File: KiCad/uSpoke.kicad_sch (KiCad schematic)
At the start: 68 parts, among them J1 SM12B-SRSS-TB, J12 Amphenol 132289, J2 PLS-1x3, J4 PLS-1x3, Q2 AO3407A, Q3 AO3400, Q5 AO3400, U1 SP0503BAHTG, U2 TP4056, U4 LM3671MF-3.3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

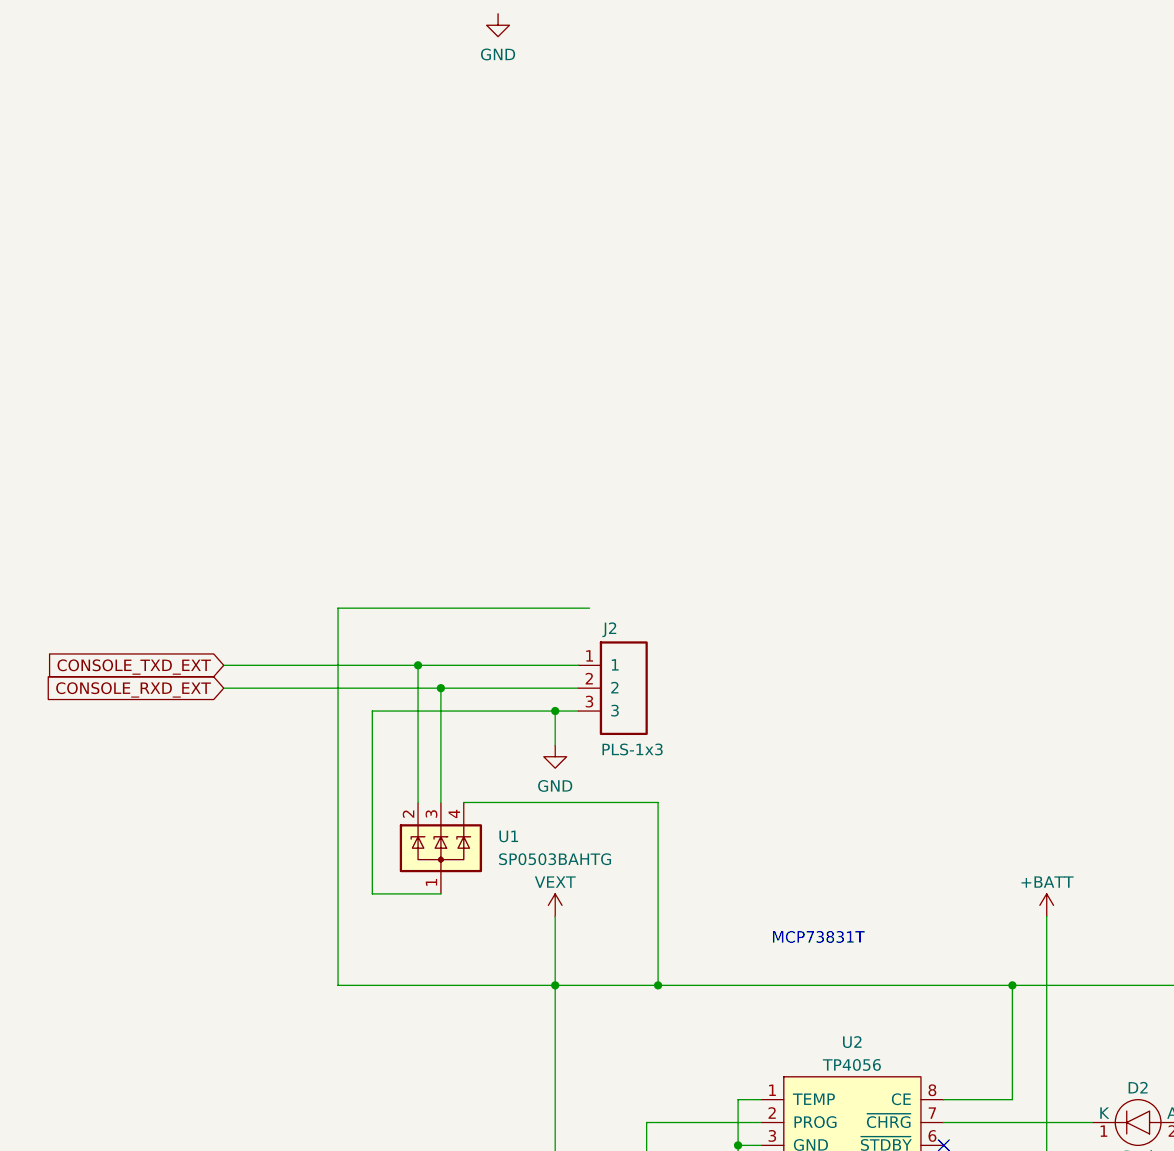
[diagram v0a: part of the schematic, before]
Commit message: Add 1x4 header (magnetic pogo)
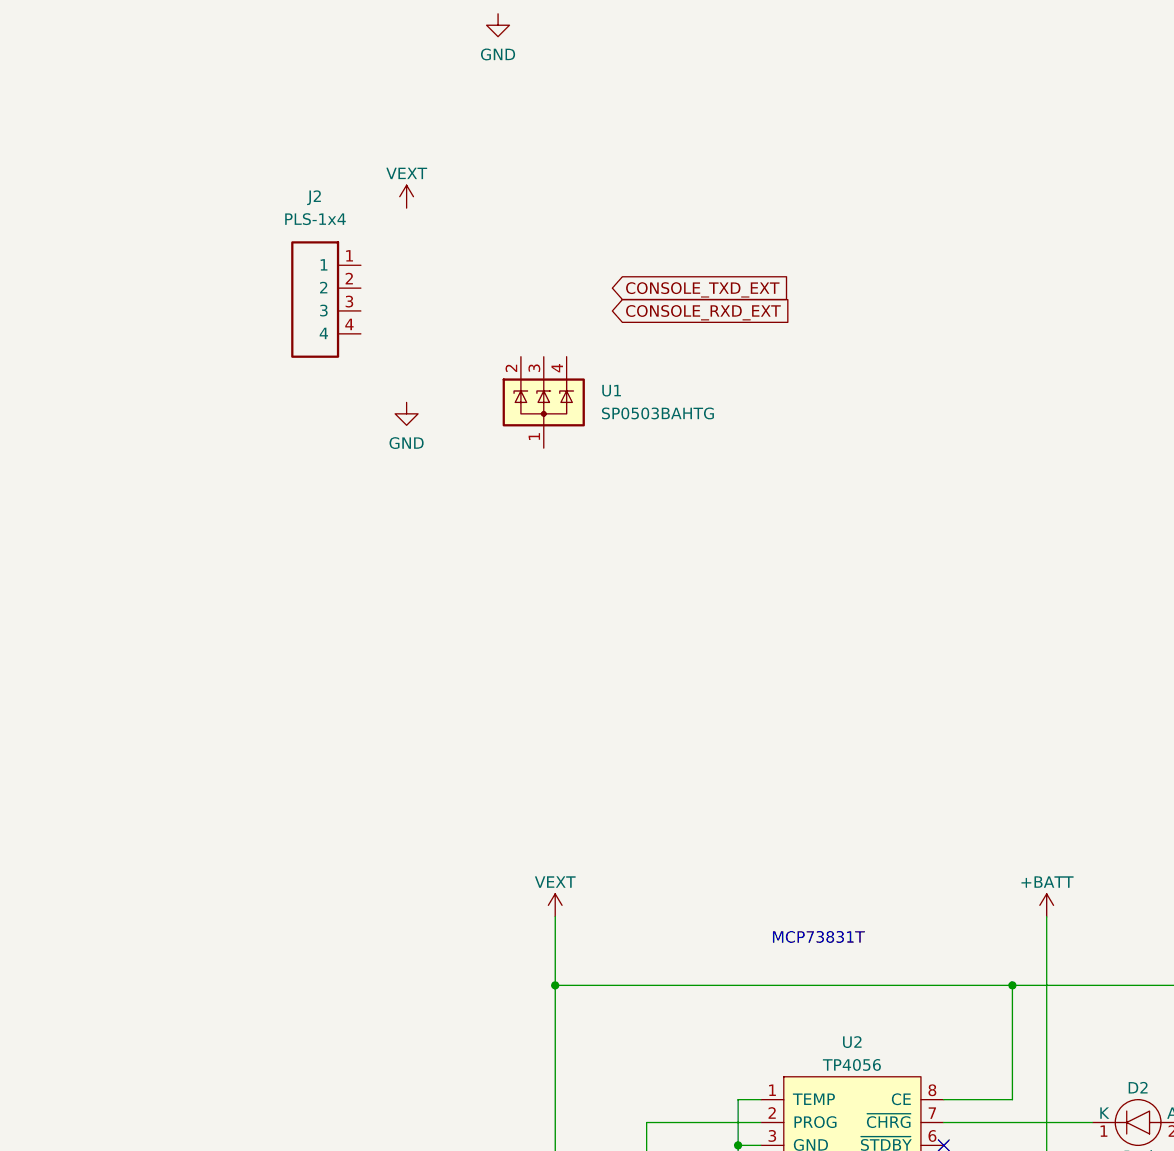
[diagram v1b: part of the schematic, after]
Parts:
- removed J2: PLS-1x3, Spoke:Header_1x3, symbol Spoke:PLS-1x3
- added J2: PLS-1x4, symbol uSpoke:PLS-1x4
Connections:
- net CONSOLE_RXD_EXT: no longer U1.3 (K)
- net CONSOLE_TXD_EXT: no longer U1.2 (K)
- net GND: no longer U1.1 (A)
- net VEXT: no longer U1.4 (K)
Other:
- moved on the sheet: U1

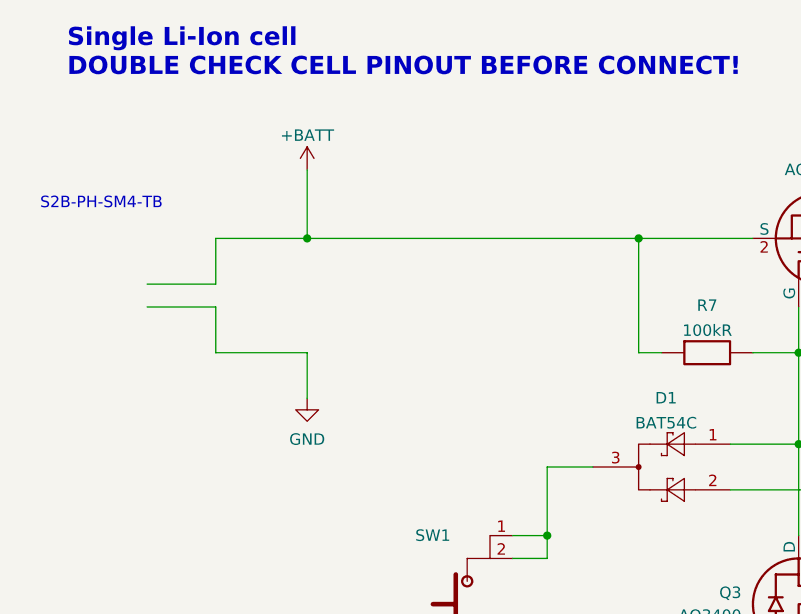
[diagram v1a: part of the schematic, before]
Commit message: Update SMA
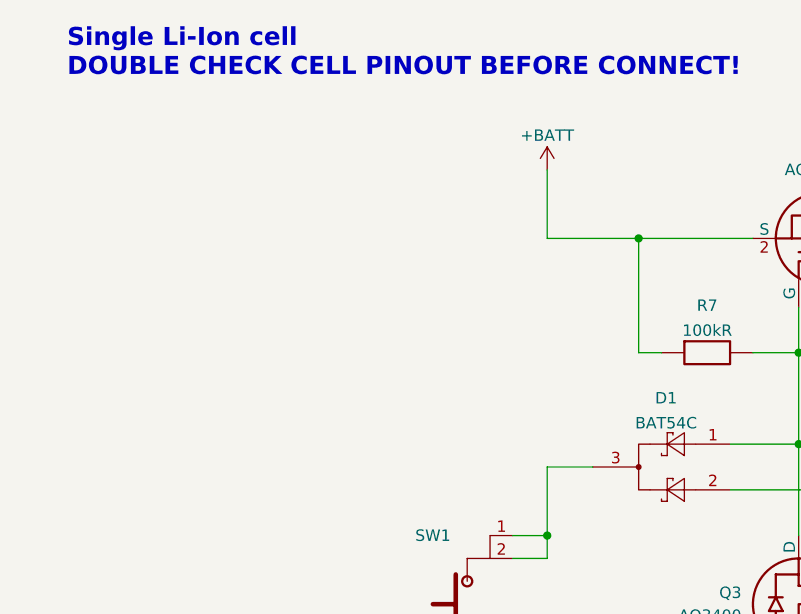
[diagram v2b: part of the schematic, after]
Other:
- note removed: "S2B-PH-SM4-TB"
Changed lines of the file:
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@@
 		)
 	)
-	(text "S2B-PH-SM4-TB"
-		(exclude_from_sim no)
-		(at 35.56 41.91 0)
-		(effects
-			(font
-				(size 1.27 1.27)
-			)
-		)
-	)
 	(text_box "Passive Buzzer\n\nIf Piezo: Populate resistor only\nIf Magnetic: Populate diode only"
 		(exclude_from_sim no)
@@
 	)
 	(junction
-		(at 58.42 45.72)
-		(diameter 0)
-		(color 0 0 0 0)
-	)
-	(junction
 		(at 330.2 228.6)
 		(diameter 0)
@@
 	(wire
 		(pts
-			(xy 48.26 58.42) (xy 58.42 58.42)
-		)
-		(stroke
-			(width 0)
-			(type default)
-		)
-	)
-	(wire
-		(pts
 			(xy 373.38 119.38) (xy 377.19 119.38)
 		)
@@
 	(wire
 		(pts
-			(xy 40.64 53.34) (xy 48.26 53.34)
-		)
-		(stroke
-			(width 0)
-			(type default)
-		)
-	)
-	(wire
-		(pts
 			(xy 334.01 73.66) (xy 337.82 73.66)
 		)
@@
 	(wire
 		(pts
-			(xy 48.26 53.34) (xy 48.26 58.42)
-		)
-		(stroke
-			(width 0)
-			(type default)
-		)
-	)
-	(wire
-		(pts
 			(xy 199.39 344.17) (xy 220.98 344.17)
 		)
@@
 	(wire
 		(pts
-			(xy 48.26 45.72) (xy 58.42 45.72)
-		)
-		(stroke
-			(width 0)
-			(type default)
-		)
-	)
-	(wire
-		(pts
 			(xy 74.93 354.33) (xy 97.79 354.33)
 		)
@@
 	(wire
 		(pts
-			(xy 58.42 45.72) (xy 95.25 45.72)
+			(xy 85.09 45.72) (xy 95.25 45.72)
 		)
 		(stroke
@@
 	(wire
 		(pts
-			(xy 40.64 50.8) (xy 48.26 50.8)
-		)
-		(stroke
-			(width 0)
-			(type default)
-		)
-	)
-	(wire
-		(pts
 			(xy 334.01 71.12) (xy 337.82 71.12)
 		)
@@
 	(wire
 		(pts
-			(xy 58.42 58.42) (xy 58.42 63.5)
-		)
-		(stroke
-			(width 0)
-			(type default)
-		)
-	)
-	(wire
-		(pts
 			(xy 330.2 226.06) (xy 330.2 228.6)
 		)
@@
 	(wire
 		(pts
-			(xy 48.26 50.8) (xy 48.26 45.72)
-		)
-		(stroke
-			(width 0)
-			(type default)
-		)
-	)
-	(wire
-		(pts
 			(xy 488.95 233.68) (xy 488.95 236.22)
 		)
@@
 	(wire
 		(pts
-			(xy 58.42 38.1) (xy 58.42 45.72)
+			(xy 85.09 38.1) (xy 85.09 45.72)
 		)
 		(stroke
@@
 	(symbol
 		(lib_id "power:+BATT")
-		(at 58.42 38.1 0)
+		(at 85.09 38.1 0)
 		(unit 1)
 		(exclude_from_sim no)
@@
 		(dnp no)
 		(property "Reference" "#PWR02"
-			(at 58.42 41.91 0)
+			(at 85.09 41.91 0)
 			(effects
 				(font
@@
 		)
 		(property "Value" "+BATT"
-			(at 58.42 34.29 0)
+			(at 85.09 34.29 0)
 			(effects
 				(font
@@
 		)
 		(property "Footprint" ""
-			(at 58.42 38.1 0)
+			(at 85.09 38.1 0)
 			(effects
 				(font
@@
 		)
 		(property "Datasheet" ""
-			(at 58.42 38.1 0)
+			(at 85.09 38.1 0)
 			(effects
 				(font
@@
 		)
 		(property "Description" "Power symbol creates a global label with name \"+BATT\""
-			(at 58.42 38.1 0)
+			(at 85.09 38.1 0)
 			(effects
 				(font
@@
 					(unit 1)
 				)
-			)
-		)
-	)
-	(symbol
-		(lib_id "power:GND")
-		(at 58.42 63.5 0)
-		(unit 1)
-		(exclude_from_sim no)
-		(in_bom yes)
-		(on_board yes)
-		(dnp no)
-		(fields_autoplaced yes)
-		(property "Reference" "#PWR03"
-			(at 58.42 69.85 0)
-			(effects
-				(font
-					(size 1.27 1.27)
-				)
-				(hide yes)
-			)
-		)
-		(property "Value" "GND"
-			(at 58.42 68.0625 0)
-			(effects
-				(font
-					(size 1.27 1.27)
-				)
-			)
-		)
-		(property "Footprint" ""
-			(at 58.42 63.5 0)
-			(effects
-				(font
-					(size 1.27 1.27)
-				)
-				(hide yes)
-			)
-		)
-		(property "Datasheet" ""
-			(at 58.42 63.5 0)
-			(effects
-				(font
-					(size 1.27 1.27)
-				)
-				(hide yes)
-			)
-		)
-		(property "Description" ""
-			(at 58.42 63.5 0)
-			(effects
-				(font
-					(size 1.27 1.27)
-				)
-			)
-		)
-		(pin "1"
-		)
-		(instances
-			(project ""
-				(path "/e63e39d7-6ac0-4ffd-8aa3-1841a4541b55"
-					(reference "#PWR03")
-					(unit 1)
-				)

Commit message: Replace charger IC
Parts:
- removed U2: TP4056, Spoke:SOIC-8-EP, symbol Spoke:TP4056
- added TP1, TP2, TP3: Pad-Round, Spoke:Pad_round, symbol Spoke:Pad-Round
- added U2: MCP73831T-2ACI/OT, symbol uSpoke:MCP73831T-2ACI/OT
- R4: value 3.9kR -> 2.0kR
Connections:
- net +BATT: now also U2.6 (VBAT)
- net GND: now also R4.2, TP3.1, U2.2 (VSS); no longer R4.1
- net VEXT: now also U2.4 (VDD)
- net at D2.1 (K): now also U2.1 (STAT)
- net I2C_SCL: now reaches U6.42 (PB6)
- net I2C_SCL: now also TP2.1
- net I2C_SDA: now reaches U6.43 (PB7)
- net I2C_SDA: now also TP1.1
- new net: R4.1, U2.5 (PROG)
- no-connect marks 5 -> 4
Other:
- note removed: "MCP73831T"
- moved on the sheet: C1, C5, D2, R10, R4

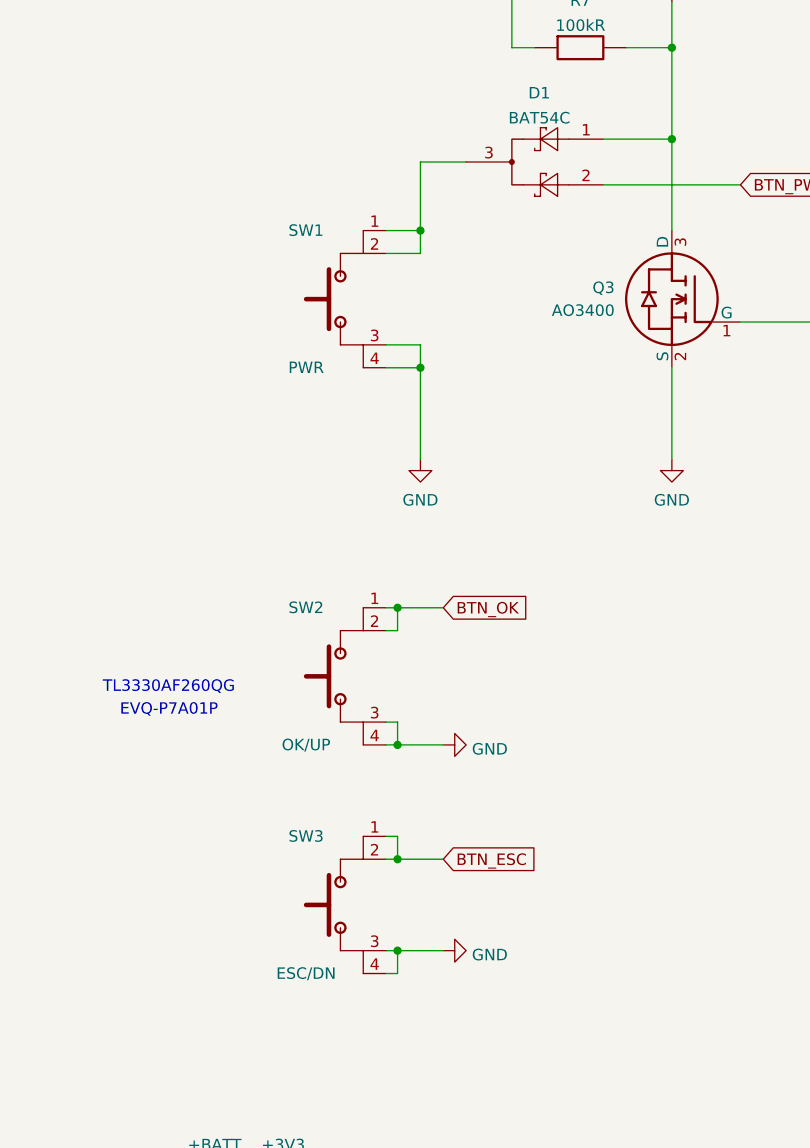
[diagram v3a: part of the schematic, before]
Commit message: Add button
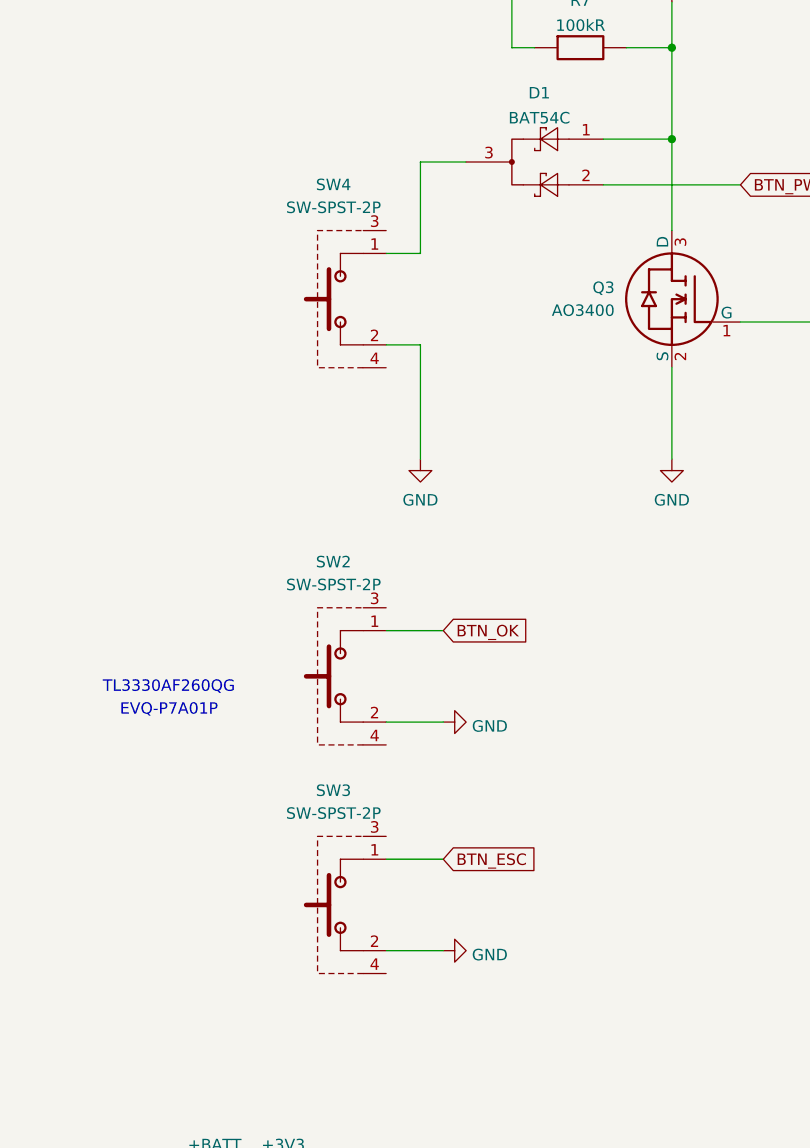
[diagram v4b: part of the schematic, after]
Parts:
- removed SW1, SW2, SW3: ~, Spoke:Button_6x6, symbol Spoke:Button-SPST-NO
- added SW2, SW3, SW4: SW-SPST-2P, symbol uSpoke:SW-SPST-2P
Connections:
- net BTN_ESC: now also SW3.1
- net BTN_OK: now also SW2.1
- net GND: now also SW2.2, SW3.2, SW4.2
- net at D1.3: now also SW4.1

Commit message: Assign footprints
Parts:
- removed SW5: ~, Spoke:Button_6x6, symbol Spoke:Button-SPST-NO
- added SW1: SW-SPST-2P, uSpoke:TL3330AF260QG, symbol uSpoke:SW-SPST-2P
- A1: footprint Spoke:E104-BT5005A -> uSpoke:E104-BT5005A
- A2: footprint Spoke:E22 -> uSpoke:E22
- C1, C13, C5, C8: footprint Spoke:C1206 -> uSpoke:C0805
- C11, C15, C16, C17, C18, C19, C20, C22, C23, C27, C30: footprint Spoke:C0603 -> uSpoke:C0603
- C14, C25, C26, C28: footprint Spoke:C_tantA -> uSpoke:C_tantA
- D1, D3, Q2, Q3, Q5: footprint Spoke:SOT-23 -> uSpoke:SOT-23
- D2, D4, D5: footprint Spoke:LED_3mm -> uSpoke:LED0603
- J1: footprint (none) -> uSpoke:SM12B-SRSS-TB
- J12: footprint Spoke:SMA -> uSpoke:SMA
- J2: footprint (none) -> uSpoke:Header_1x4
- J4: footprint Spoke:Header_1x3 -> uSpoke:Header_1x3
- L1: footprint Spoke:L1616 -> uSpoke:L1616
- R1, R10, R11, R12, R13, R15, R17, R23, R26, R27, R28, R29, R3, R32, R33, R34, R4, R5, R6, R7, R8, R9: footprint Spoke:R0603 -> uSpoke:R0603
- SW2, SW3, SW4: footprint (none) -> uSpoke:TL3330AF260QG
- TP1, TP10, TP11, TP2, TP3: footprint Spoke:Pad_round -> uSpoke:Pad_round
- U1: footprint Spoke:SOT-23-5 -> uSpoke:SOT-143
- U2: footprint (none) -> uSpoke:SOT-23-5
- U4: footprint Spoke:SOT-23-5 -> uSpoke:SOT-23-5
- U5: footprint Spoke:TSSOP-16 -> uSpoke:TSSOP-16
- U6: footprint Spoke:LQFP-48 -> uSpoke:LQFP-48
- X1: footprint Spoke:Xtal_3225 -> uSpoke:Xtal_3225
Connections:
- net +3V3: now also SW1.1
- net BOOT0: now also SW1.4 (1)
